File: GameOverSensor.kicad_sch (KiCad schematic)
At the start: 31 parts

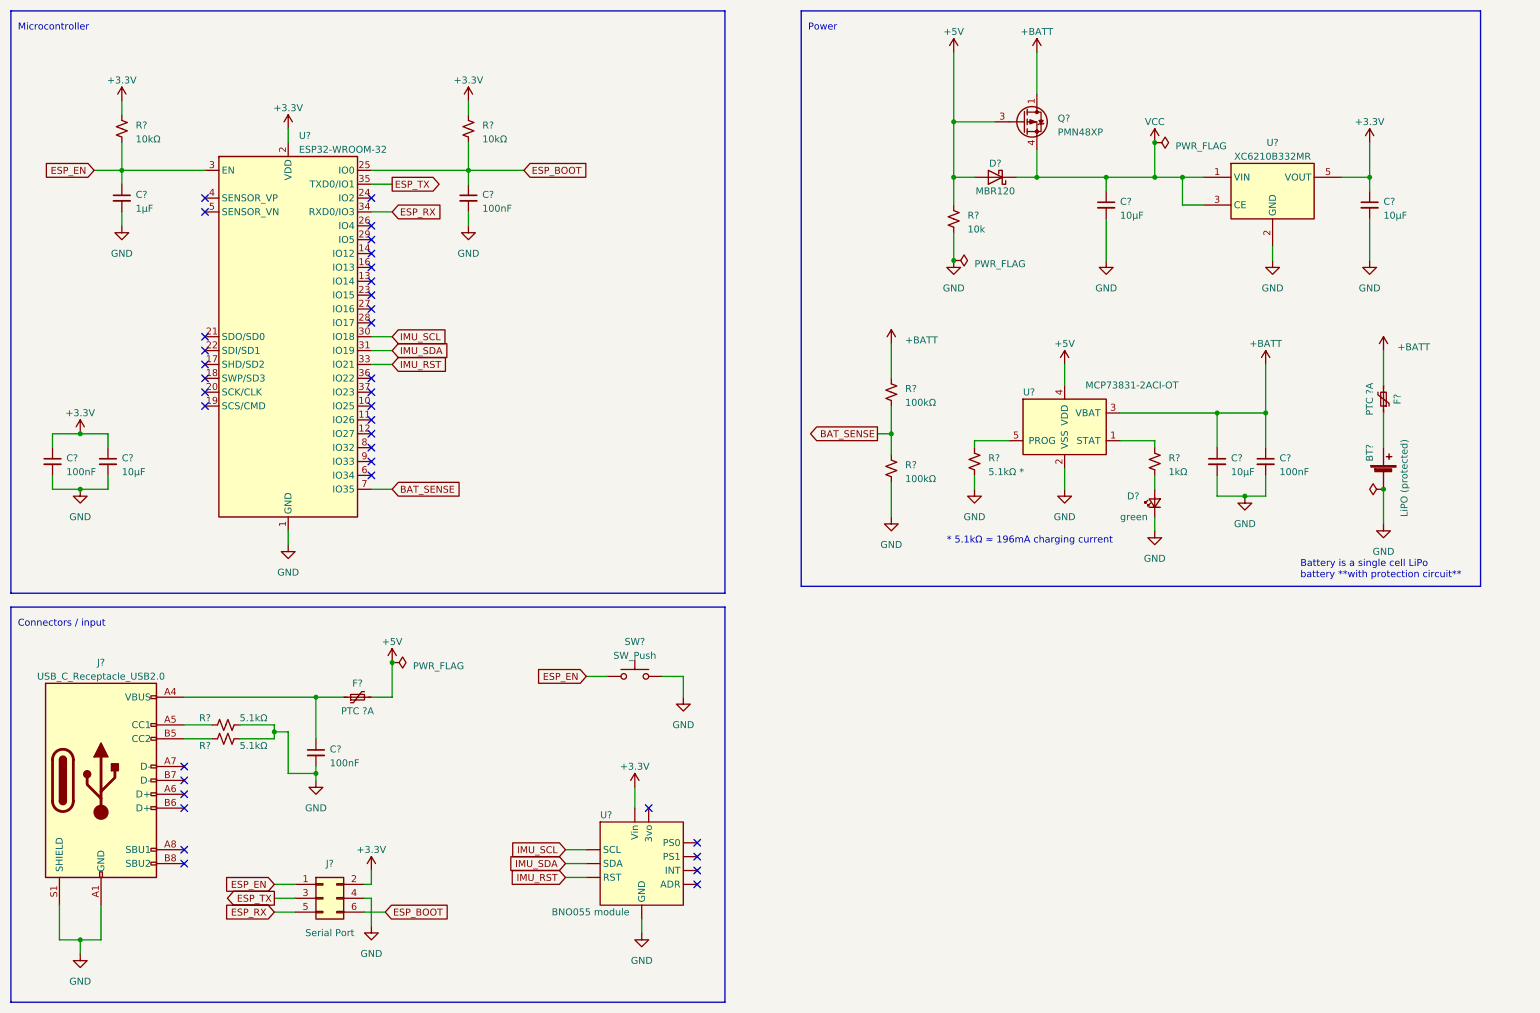
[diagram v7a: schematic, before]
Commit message: Adds LEDs to indicate battery level
I used RGB LEDs instead of 3 different LEDs for no specific reason, that
should be easy to change later if we prefer.

1K resistors were chosen to have dim LEDs on purpose, this value can be
adjusted to whatever makes sense later.
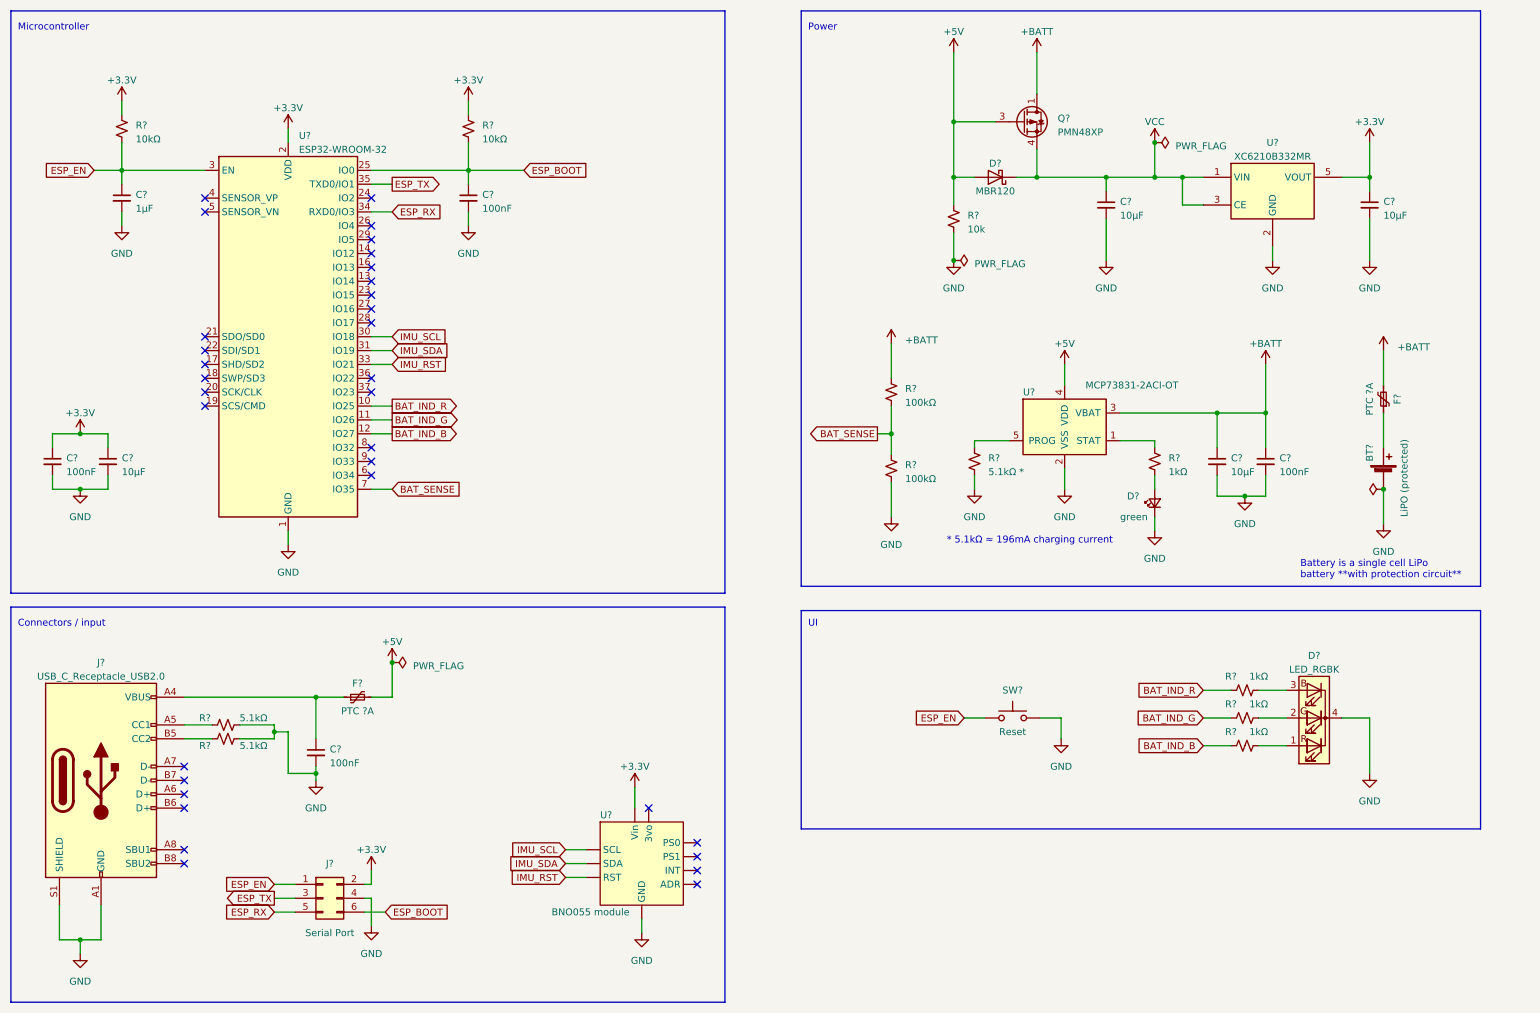
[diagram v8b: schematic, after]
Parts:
- added D?: LED_RGBK, symbol Device:LED_RGBK
- added R? (x3): 1kΩ, symbol Device:R_Small_US
- SW?: value SW_Push -> Reset
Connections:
- net GND: now also D?.4 (K)
- net BAT_IND_R: now reaches U?.10 (IO25)
- net BAT_IND_R: now also R?.1
- net BAT_IND_G: now reaches U?.11 (IO26)
- net BAT_IND_G: now also R?.1
- net BAT_IND_B: now reaches U?.12 (IO27)
- net BAT_IND_B: now also R?.1
- new net: D?.1 (RA), R?.2
- new net: D?.3 (BA), R?.2
- new net: D?.2 (GA), R?.2
- no-connect marks 36 -> 33
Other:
- note added: "UI"
- moved on the sheet: SW?
